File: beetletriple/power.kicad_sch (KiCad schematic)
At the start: 15 parts, among them U1 LM2596S-ADJ, U2 HT7550-1

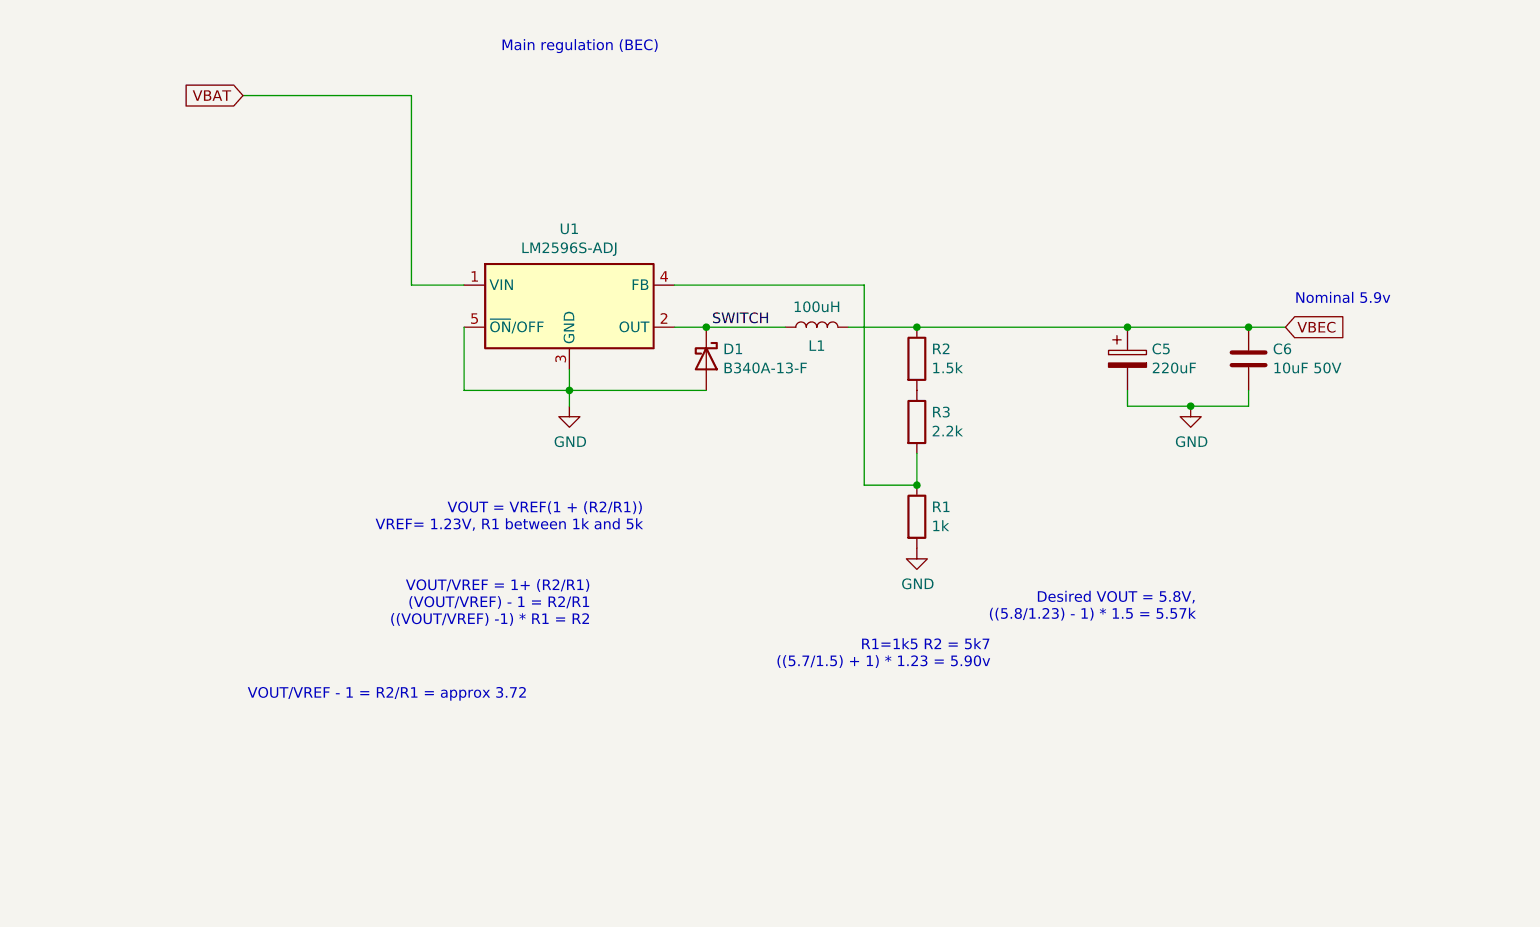
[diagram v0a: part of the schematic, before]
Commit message: Beetleweight triple: redo the power and passives
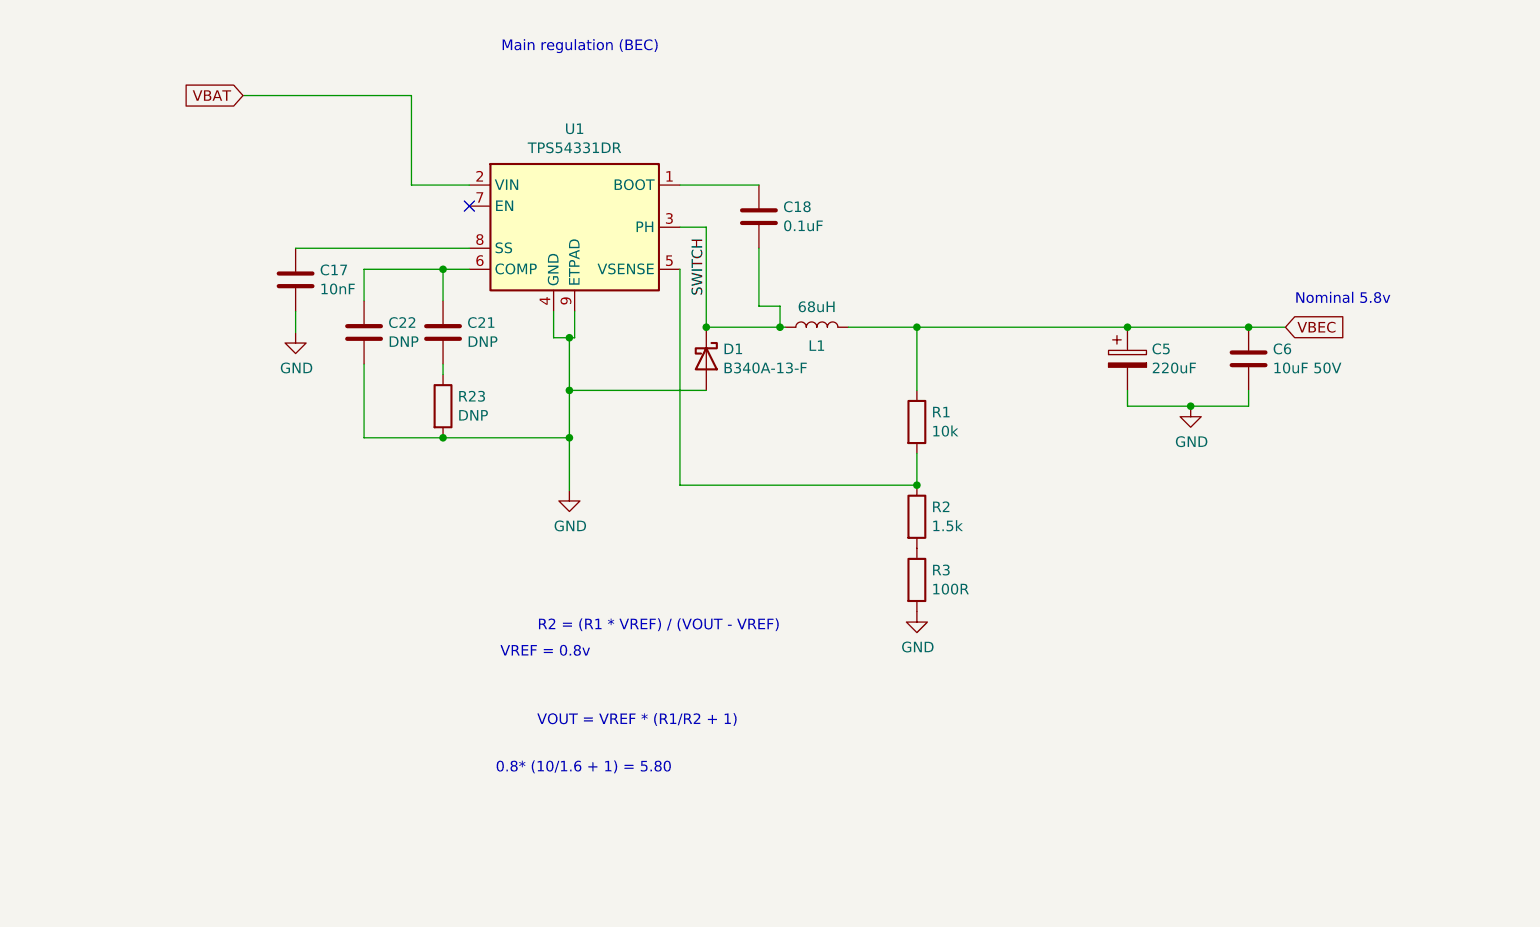
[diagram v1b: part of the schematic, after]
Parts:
- removed U1: LM2596S-ADJ, Package_TO_SOT_SMD:TO-263-5_TabPin3, symbol Regulator_Switching:LM2596S-ADJ
- added C17: 10nF, Capacitor_SMD:C_1206_3216Metric, symbol Device:C
- added C18: 0.1uF, Capacitor_SMD:C_1206_3216Metric, symbol Device:C
- added C21, C22: DNP, Capacitor_SMD:C_1206_3216Metric, symbol Device:C
- added R23: DNP, Resistor_SMD:R_0805_2012Metric, symbol Device:R
- added U1: TPS54331DR, Package_SO:TI_SO-PowerPAD-8_ThermalVias, symbol Regulator_Switching:TPS54336ADDA
- L1: value 100uH -> 68uH; LCSC C497890 -> C286354
- R1: value 1k -> 10k
- R3: value 2.2k -> 100R
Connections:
- net GND: now also R3.2, C17.2, C22.2, R23.2, U1.4 (GND), U1.9 (ETPAD); no longer R1.2
- net SWITCH: now also C18.2, U1.3 (PH)
- net VBAT: now also U1.2 (VIN)
- net VBEC: now also R1.1; no longer R2.1
- new net: C21.1, C22.1, U1.6 (COMP)
- new net: C21.2, R23.1
- new net: R1.2, R2.1, U1.5 (VSENSE)
- new net: C18.1, U1.1 (BOOT)
- new net: C17.1, U1.8 (SS)
- no-connect marks 0 -> 1
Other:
- note added: "0.8* (10/1.6 + 1) = 5.80"
- note added: "Nominal 5.8v"
- note added: "R2 = (R1 * VREF) / (VOUT - VREF)"
- note added: "VOUT = VREF * (R1/R2 + 1)"
- note added: "VREF = 0.8v"
- note removed: "Desired VOUT = 5.8V, ((5.8/1.23) - 1) * 1.5 = 5.57k"
- note removed: "Nominal 5.9v"
- note removed: "R1=1k5 R2 = 5k7 ((5.7/1.5) + 1) * 1.23 = 5.90v"
- note removed: "VOUT = VREF(1 + (R2/R1)) VREF= 1.23V, R1 between 1k and 5k"
- note removed: "VOUT/VREF - 1 = R2/R1 = approx 3.72"
- note removed: "VOUT/VREF = 1+ (R2/R1) (VOUT/VREF) - 1 = R2/R1 ((VOUT/VREF) -1) * R1 = R2"
- moved on the sheet: R1, R2

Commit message: Beetleweight triple: more.
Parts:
- L1: value 68uH -> 10uH; LCSC C286354 -> (none)
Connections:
- net COMP: now reaches C21.1, C22.1, U1.6 (COMP)
- net REG_SENSE: now reaches R1.2, R2.1, U1.5 (VSENSE)
- net REG_BOOT: now reaches C18.1, U1.1 (BOOT)
- net REG_SOFTSTART: now reaches C17.1, U1.8 (SS)
- net SWITCH renamed REG_PH
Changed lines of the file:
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@@
     (effects (font (size 1.27 1.27)) (justify right bottom))
   )
-  (label "SWITCH" (at 184.785 57.15 90)
+  (label "REG_SOFTSTART" (at 150.495 51.435 180)
+    (effects (font (size 1.27 1.27)) (justify right bottom))
+  )
+  (label "COMP" (at 150.495 53.975 180)
+    (effects (font (size 1.27 1.27)) (justify right bottom))
+  )
+  (label "REG_PH" (at 184.785 59.055 90)
     (effects (font (size 1.27 1.27)) (justify left bottom))
+  )
+  (label "REG_BOOT" (at 190.5 43.815 180)
+    (effects (font (size 1.27 1.27)) (justify right bottom))
+  )
+  (label "REG_SENSE" (at 198.12 80.01 180)
+    (effects (font (size 1.27 1.27)) (justify right bottom))
   )
   (global_label "VBAT_IN_1" (shape input) (at 28.575 38.735 180)
@@
     (in_bom yes) (on_board yes)
     (property "Reference" "L1" (id 0) (at 198.12 63.2268 90))
-    (property "Value" "68uH" (id 1) (at 198.12 58.5405 90))
+    (property "Value" "10uH" (id 1) (at 198.12 58.5405 90))
     (property "Footprint" "Inductor_SMD:L_12x12mm_H4.5mm" (id 2) (at 198.12 60.96 0)
       (effects (font (size 1.27 1.27)) hide)
@@
       (effects (font (size 1.27 1.27)) hide)
     )
-    (property "LCSC" " C286354" (id 4) (at 198.12 60.96 90)
+    (property "LCSC" "" (id 4) (at 198.12 60.96 90)
       (effects (font (size 1.27 1.27)) hide)
     )

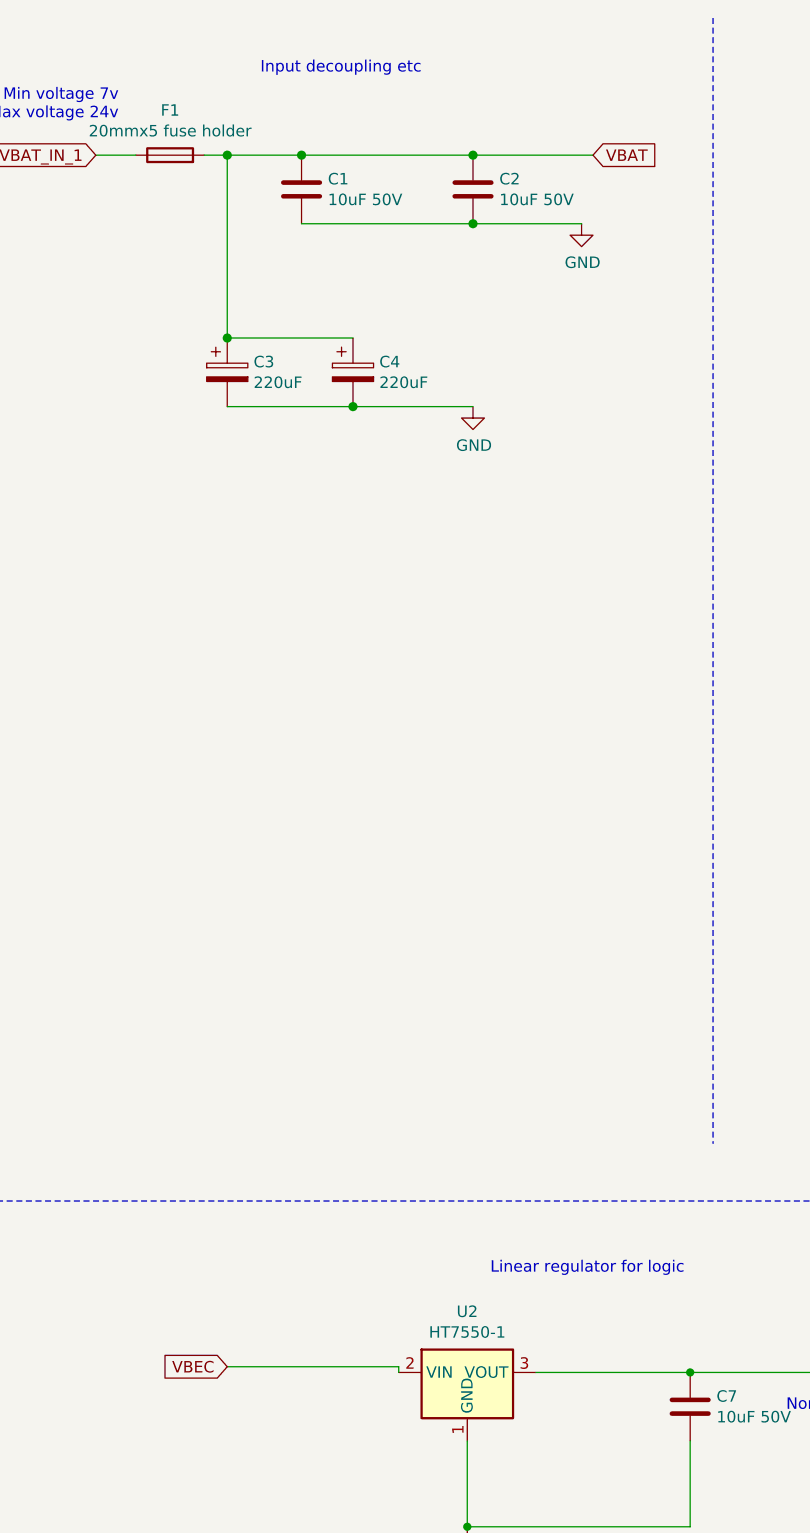
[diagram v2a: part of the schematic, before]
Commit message: Pin swaps and routing
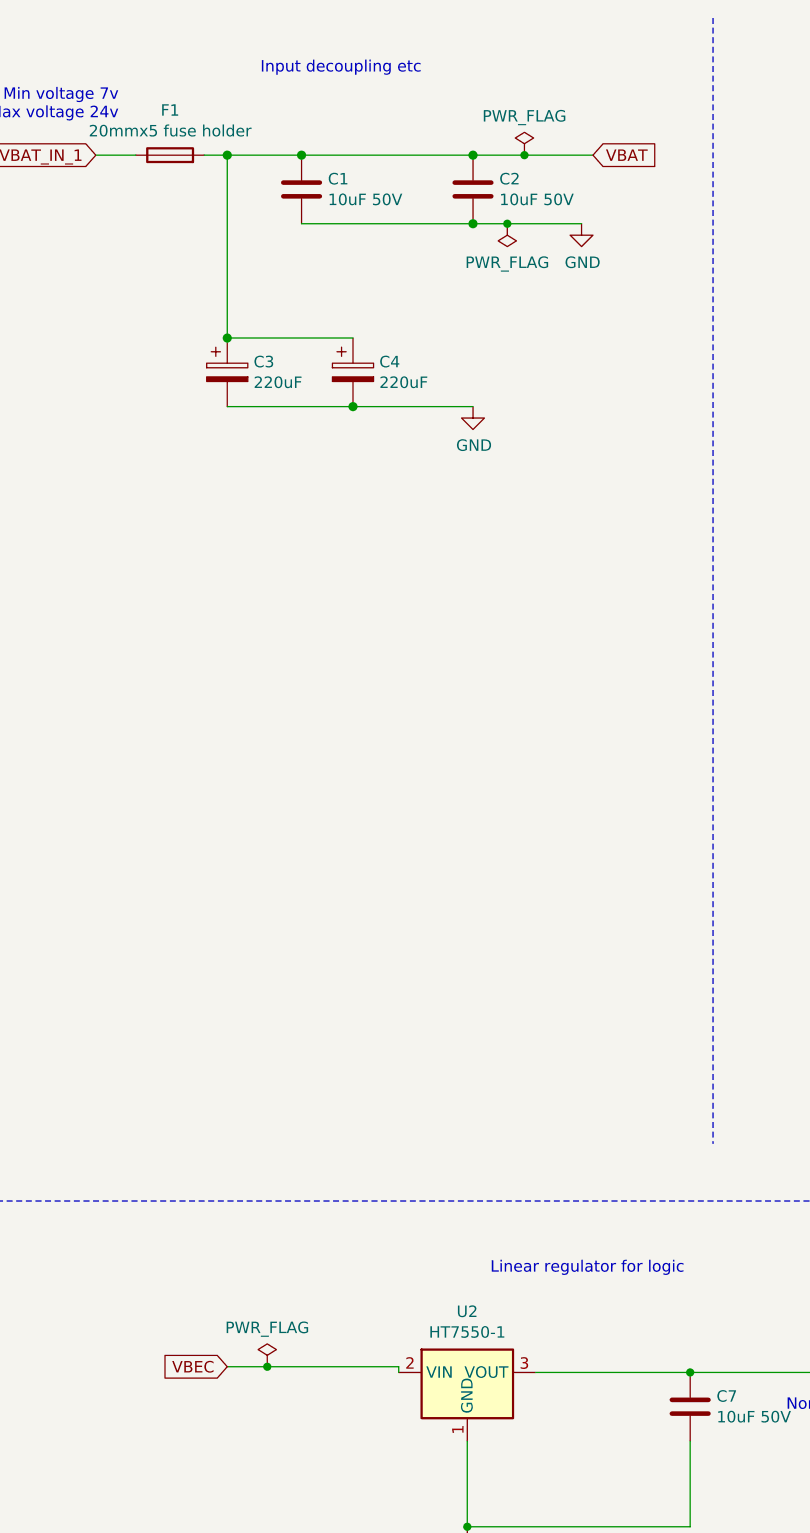
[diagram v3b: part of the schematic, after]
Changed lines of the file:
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@@
   (junction (at 43.18 38.735) (diameter 1.016) (color 0 0 0 0))
   (junction (at 43.18 59.055) (diameter 1.016) (color 0 0 0 0))
+  (junction (at 47.625 173.355) (diameter 0.9144) (color 0 0 0 0))
   (junction (at 51.435 38.735) (diameter 1.016) (color 0 0 0 0))
   (junction (at 57.15 66.675) (diameter 1.016) (color 0 0 0 0))
@@
   (junction (at 70.485 38.735) (diameter 1.016) (color 0 0 0 0))
   (junction (at 70.485 46.355) (diameter 1.016) (color 0 0 0 0))
+  (junction (at 74.295 46.355) (diameter 0.9144) (color 0 0 0 0))
+  (junction (at 76.2 38.735) (diameter 0.9144) (color 0 0 0 0))
   (junction (at 94.615 173.99) (diameter 0.9144) (color 0 0 0 0))
   (junction (at 153.035 53.975) (diameter 0.9144) (color 0 0 0 0))
@@
     (stroke (width 0) (type solid) (color 0 0 0 0))
   )
-  (wire (pts (xy 43.18 173.355) (xy 62.23 173.355))
+  (wire (pts (xy 43.18 173.355) (xy 47.625 173.355))
+    (stroke (width 0) (type solid) (color 0 0 0 0))
+  )
+  (wire (pts (xy 47.625 173.355) (xy 62.23 173.355))
     (stroke (width 0) (type solid) (color 0 0 0 0))
   )
@@
     (stroke (width 0) (type solid) (color 0 0 0 0))
   )
-  (wire (pts (xy 70.485 38.735) (xy 83.82 38.735))
-    (stroke (width 0) (type solid) (color 0 0 0 0))
-  )
-  (wire (pts (xy 70.485 46.355) (xy 82.55 46.355))
+  (wire (pts (xy 70.485 38.735) (xy 76.2 38.735))
+    (stroke (width 0) (type solid) (color 0 0 0 0))
+  )
+  (wire (pts (xy 70.485 46.355) (xy 74.295 46.355))
+    (stroke (width 0) (type solid) (color 0 0 0 0))
+  )
+  (wire (pts (xy 74.295 46.355) (xy 82.55 46.355))
+    (stroke (width 0) (type solid) (color 0 0 0 0))
+  )
+  (wire (pts (xy 76.2 38.735) (xy 83.82 38.735))
     (stroke (width 0) (type solid) (color 0 0 0 0))
   )
@@
     )
   )
+  (symbol (lib_id "power:PWR_FLAG") (at 47.625 173.355 0) (unit 1)
+    (in_bom yes) (on_board yes)
+    (property "Reference" "#FLG0102" (id 0) (at 47.625 171.45 0)
+      (effects (font (size 1.27 1.27)) hide)
+    )
+    (property "Value" "PWR_FLAG" (id 1) (at 47.625 169.0306 0))
+    (property "Footprint" "" (id 2) (at 47.625 173.355 0)
+      (effects (font (size 1.27 1.27)) hide)
+    )
+    (property "Datasheet" "~" (id 3) (at 47.625 173.355 0)
+      (effects (font (size 1.27 1.27)) hide)
+    )
+    (pin "1")
+  )
+  (symbol (lib_id "power:PWR_FLAG") (at 74.295 46.355 180) (unit 1)
+    (in_bom yes) (on_board yes)
+    (property "Reference" "#FLG?" (id 0) (at 74.295 48.26 0)
+      (effects (font (size 1.27 1.27)) hide)
+    )
+    (property "Value" "PWR_FLAG" (id 1) (at 74.295 50.6794 0))
+    (property "Footprint" "" (id 2) (at 74.295 46.355 0)
+      (effects (font (size 1.27 1.27)) hide)
+    )
+    (property "Datasheet" "~" (id 3) (at 74.295 46.355 0)
+      (effects (font (size 1.27 1.27)) hide)
+    )
+    (pin "1")
+  )
+  (symbol (lib_id "power:PWR_FLAG") (at 76.2 38.735 0) (unit 1)
+    (in_bom yes) (on_board yes)
+    (property "Reference" "#FLG0101" (id 0) (at 76.2 36.83 0)
+      (effects (font (size 1.27 1.27)) hide)
+    )
+    (property "Value" "PWR_FLAG" (id 1) (at 76.2 34.4106 0))
+    (property "Footprint" "" (id 2) (at 76.2 38.735 0)
+      (effects (font (size 1.27 1.27)) hide)
+    )
+    (property "Datasheet" "~" (id 3) (at 76.2 38.735 0)
+      (effects (font (size 1.27 1.27)) hide)
+    )
+    (pin "1")
+  )
   (symbol (lib_id "Device:L") (at 198.12 60.96 90) (unit 1)
